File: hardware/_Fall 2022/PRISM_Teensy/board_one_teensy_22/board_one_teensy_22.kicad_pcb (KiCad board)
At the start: 2 copper layers, 61 x 88.9 mm, 20 parts, among them J1 EAST, J2 CORE_IO, J3 USB_micro, U1 Teensy4.1, U2 BNO055_Breakout, U3 3966

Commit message: minor fixes
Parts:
- moved ? 0.25 mm to (138.2, 134.6)
- moved H3 0.10 mm to (156.7, 53.2)
- moved H4 0.09 mm to (118.6, 135.8)
- moved H2 0.09 mm to (156.7, 135.8)
- moved H1 0.08 mm to (118.6, 53.3)
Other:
- outline, holes or cut-outs redrawn
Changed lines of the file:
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@@
     (descr "Resistor SMD 0603 (1608 Metric), square (rectangular) end terminal, IPC_7351 nominal, (Body size source: IPC-SM-782 page 72, https://www.pcb-3d.com/wordpress/wp-content/uploads/ipc-sm-782a_amendment_1_and_2.pdf), generated with kicad-footprint-generator")
     (tags "resistor")
-    (property "JLC" "C473494")
     (property "Sheetfile" "board_one_teensy_22.kicad_sch")
     (property "Sheetname" "")
+    (property "Vendor" "C23024")
     (attr smd)
     (fp_text reference "R5" (at 0 -1.43 90) (layer "F.SilkS") hide
@@
     (property "sensor output" "I2C,SPI")
     (attr through_hole)
-    (fp_text reference "U3" (at -12.7 -9.69 90) (layer "F.SilkS")
+    (fp_text reference "U3" (at -5.332 -0.048 90) (layer "F.SilkS")
       (effects (font (size 1 1) (thickness 0.15)) (justify left))
     )
@@
   )
   (footprint "MountingHole:MountingHole_3.2mm_M3_DIN965_Pad_TopBottom" (layer "F.Cu")
-    (at 118.618 53.34)
+    (at 118.614971 53.255682)
     (descr "Mounting Hole 3.2mm, M3, DIN965")
     (tags "mounting hole 3.2mm m3 din965")
@@
     (property "Sheetname" "")
     (attr through_hole)
-    (fp_text reference "J2" (at 3.275 -4.765 90) (layer "F.SilkS")
-      (effects (font (size 1 1) (thickness 0.15)))
-    )
-    (fp_text value "CORE_IO" (at 6 7.45 90) (layer "F.Fab")
+    (fp_text reference "J2" (at -3.724 2.758 90) (layer "F.SilkS")
+      (effects (font (size 1 1) (thickness 0.15)))
+    )
+    (fp_text value "CORE_IO" (at 6 7.838 90) (layer "F.SilkS")
       (effects (font (size 1 1) (thickness 0.15)))
     )
@@
     (descr "Capacitor SMD 0603 (1608 Metric), square (rectangular) end terminal, IPC_7351 nominal, (Body size source: IPC-SM-782 page 76, https://www.pcb-3d.com/wordpress/wp-content/uploads/ipc-sm-782a_amendment_1_and_2.pdf), generated with kicad-footprint-generator")
     (tags "capacitor")
-    (property "JLC" "C307380")
     (property "Sheetfile" "board_one_teensy_22.kicad_sch")
     (property "Sheetname" "")
+    (property "Vendor" "C14663")
     (attr smd)
     (fp_text reference "C2" (at 0 -1.43 90) (layer "F.SilkS") hide
@@
     (descr "Capacitor SMD 0603 (1608 Metric), square (rectangular) end terminal, IPC_7351 nominal, (Body size source: IPC-SM-782 page 76, https://www.pcb-3d.com/wordpress/wp-content/uploads/ipc-sm-782a_amendment_1_and_2.pdf), generated with kicad-footprint-generator")
     (tags "capacitor")
-    (property "JLC" "C307380")
     (property "Sheetfile" "board_one_teensy_22.kicad_sch")
     (property "Sheetname" "")
+    (property "Vendor" "C14663")
     (attr smd)
     (fp_text reference "C1" (at 0 -1.43 -90) (layer "F.SilkS") hide
@@
     (descr "SOT, 3 Pin (https://www.jedec.org/system/files/docs/to-236h.pdf variant AB), generated with kicad-footprint-generator ipc_gullwing_generator.py")
     (tags "SOT TO_SOT_SMD")
-    (property "JLC" "C369922")
     (property "Sheetfile" "board_one_teensy_22.kicad_sch")
     (property "Sheetname" "")
+    (property "Vendor" "C369922")
     (attr smd)
     (fp_text reference "D1" (at 0 -2.4 90) (layer "F.SilkS")
@@
   )
   (footprint "MountingHole:MountingHole_3.2mm_M3_DIN965_Pad_TopBottom" (layer "F.Cu")
-    (at 118.618 135.89)
+    (at 118.603304 135.797904)
     (descr "Mounting Hole 3.2mm, M3, DIN965")
     (tags "mounting hole 3.2mm m3 din965")
@@
     (property "Sheetname" "")
     (attr exclude_from_pos_files)
-    (fp_text reference "H4" (at 0 -3.8) (layer "User.1")
+    (fp_text reference "H4" (at 0 6.950096) (layer "User.1")
       (effects (font (size 1 1) (thickness 0.15)))
     )
@@
   )
   (footprint "MountingHole:MountingHole_3.2mm_M3_DIN965_Pad_TopBottom" (layer "F.Cu")
-    (at 156.718 53.34)
+    (at 156.706146 53.242782)
     (descr "Mounting Hole 3.2mm, M3, DIN965")
     (tags "mounting hole 3.2mm m3 din965")
@@
     (property "Sheetname" "")
     (attr through_hole)
-    (fp_text reference "U2" (at 0 -11.565 90) (layer "F.SilkS")
+    (fp_text reference "U2" (at 0 -0.386 90) (layer "F.SilkS")
       (effects (font (size 1 1) (thickness 0.15)))
     )
@@
     (descr "Resistor SMD 0603 (1608 Metric), square (rectangular) end terminal, IPC_7351 nominal, (Body size source: IPC-SM-782 page 72, https://www.pcb-3d.com/wordpress/wp-content/uploads/ipc-sm-782a_amendment_1_and_2.pdf), generated with kicad-footprint-generator")
     (tags "resistor")
-    (property "JLC" "C163495")
     (property "Sheetfile" "board_one_teensy_22.kicad_sch")
     (property "Sheetname" "")
+    (property "Vendor" "C25811")
     (attr smd)
     (fp_text reference "R4" (at 0 -1.43 -90) (layer "F.SilkS") hide
@@
   )
   (footprint "MountingHole:MountingHole_3.2mm_M3_DIN965_Pad_TopBottom" (layer "F.Cu")
-    (at 156.718 135.89)
+    (at 156.701211 135.804448)
     (descr "Mounting Hole 3.2mm, M3, DIN965")
     (tags "mounting hole 3.2mm m3 din965")
@@
     (property "Sheetname" "")
     (attr exclude_from_pos_files)
-    (fp_text reference "H2" (at 0 -3.8) (layer "User.1")
+    (fp_text reference "H2" (at 0.524789 6.181552) (layer "User.1")
       (effects (font (size 1 1) (thickness 0.15)))
     )
@@
   )
   (footprint "LOGO" (layer "F.Cu")
-    (at 138.43 134.62)
+    (at 138.176 134.62)
     (attr board_only exclude_from_pos_files exclude_from_bom)
     (fp_text reference "" (at 0 0) (layer "F.SilkS")
@@
     (property "Sheetname" "")
     (attr through_hole)
-    (fp_text reference "U1" (at 0 -10.16 90) (layer "F.SilkS")
+    (fp_text reference "U1" (at 6.866 -0.113 90) (layer "F.SilkS")
       (effects (font (size 1 1) (thickness 0.15)))
     )
@@
       (effects (font (size 1 1) (thickness 0.15)))
     )
-    (fp_text value "EAST" (at 3 7.45) (layer "F.Fab")
+    (fp_text value "EAST" (at 3 8.122) (layer "F.SilkS")
       (effects (font (size 1 1) (thickness 0.15)))
     )
@@
   )
   (gr_line (start 163.28 102.04) (end 163.28 127.44) (layer "Dwgs.User") (width 0.2))
+  (gr_circle (center 156.71 135.8) (end 158.54642 135.8) (layer "Dwgs.User") (width 0.2) (fill none))
   (gr_line (start 145.5 102.04) (end 163.28 102.04) (layer "Dwgs.User") (width 0.2))
+  (gr_circle (center 156.71 53.25) (end 158.54642 53.25) (layer "Dwgs.User") (width 0.2) (fill none))
   (gr_line (start 145.5 71.37) (end 165.82 71.37) (layer "Dwgs.User") (width 0.2))
+  (gr_circle (center 118.61 53.25) (end 120.44642 53.25) (layer "Dwgs.User") (width 0.2) (fill none))
   (gr_line (start 145.5 127.44) (end 145.5 102.04) (layer "Dwgs.User") (width 0.2))
   (gr_line (start 165.82 71.37) (end 165.82 98.04) (layer "Dwgs.User") (width 0.2))
@@
   (gr_line (start 119.72 86.075) (end 119.72 102.975) (layer "Dwgs.User") (width 0.2))
   (gr_line (start 145.5 98.04) (end 145.5 71.37) (layer "Dwgs.User") (width 0.2))
+  (gr_circle (center 118.61 135.8) (end 120.44642 135.8) (layer "Dwgs.User") (width 0.2) (fill none))
   (gr_line (start 111.12 102.975) (end 111.12 86.075) (layer "Dwgs.User") (width 0.2))
   (gr_line (start 141.5 119.73) (end 141.5 58.77) (layer "Dwgs.User") (width 0.2))
@@
   (gr_line (start 119.72 102.975) (end 111.12 102.975) (layer "Dwgs.User") (width 0.2))
   (gr_line (start 165.82 98.04) (end 145.5 98.04) (layer "Dwgs.User") (width 0.2))
-  (gr_circle (center 156.71 135.8) (end 158.54642 135.8) (layer "Edge.Cuts") (width 0.2) (fill none))
   (gr_line (start 142.61 123.23) (end 142.61 127.484) (layer "Edge.Cuts") (width 0.2))
   (gr_arc (start 130.11 127.484) (mid 129.23132 129.60532) (end 127.11 130.484) (layer "Edge.Cuts") (width 0.2))
   (gr_line (start 168.14 136.435) (end 168.14 52.615) (layer "Edge.Cuts") (width 0.2))
-  (gr_circle (center 156.71 53.25) (end 158.54642 53.25) (layer "Edge.Cuts") (width 0.2) (fill none))
   (gr_line (start 125.61 130.484) (end 127.11 130.484) (layer "Edge.Cuts") (width 0.2))
-  (gr_circle (center 118.61 53.25) (end 120.44642 53.25) (layer "Edge.Cuts") (width 0.2) (fill none))
   (gr_line (start 109.72 138.975) (end 165.6 138.975) (layer "Edge.Cuts") (width 0.2))
   (gr_line (start 139.61 120.23) (end 138.11 120.23) (layer "Edge.Cuts") (width 0.2))
@@
   (gr_arc (start 122.61 123.23) (mid 123.48868 121.10868) (end 125.61 120.23) (layer "Edge.Cuts") (width 0.2))
   (gr_line (start 130.11 123.23) (end 130.11 127.484) (layer "Edge.Cuts") (width 0.2))
-  (gr_circle (center 118.61 135.8) (end 120.44642 135.8) (layer "Edge.Cuts") (width 0.2) (fill none))
   (gr_line (start 122.61 127.484) (end 122.61 123.23) (layer "Edge.Cuts") (width 0.2))
   (gr_arc (start 109.72 138.975) (mid 107.923949 138.231051) (end 107.18 136.435) (layer "Edge.Cuts") (width 0.2))

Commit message: Board one complete
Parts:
- added D2: SS54, JLC_footprints:DO-214AC, F.Cu at (162.3, 61.0)
- D1: value BAT54C -> SS54; footprint Package_TO_SOT_SMD:SOT-23 -> JLC_footprints:DO-214AC
- moved D1 5.01 mm to (162.3, 65.3), turned to 180 degrees
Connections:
- U1 pad 12: /CS -> unconnected-(U1-Pad12)
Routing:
- net /VIN: track 27.0 -> 36.9 mm
- net /V_BATT: track 79.5 -> 76.3 mm
- net /V_USB: track 52.3 -> 54.2 mm

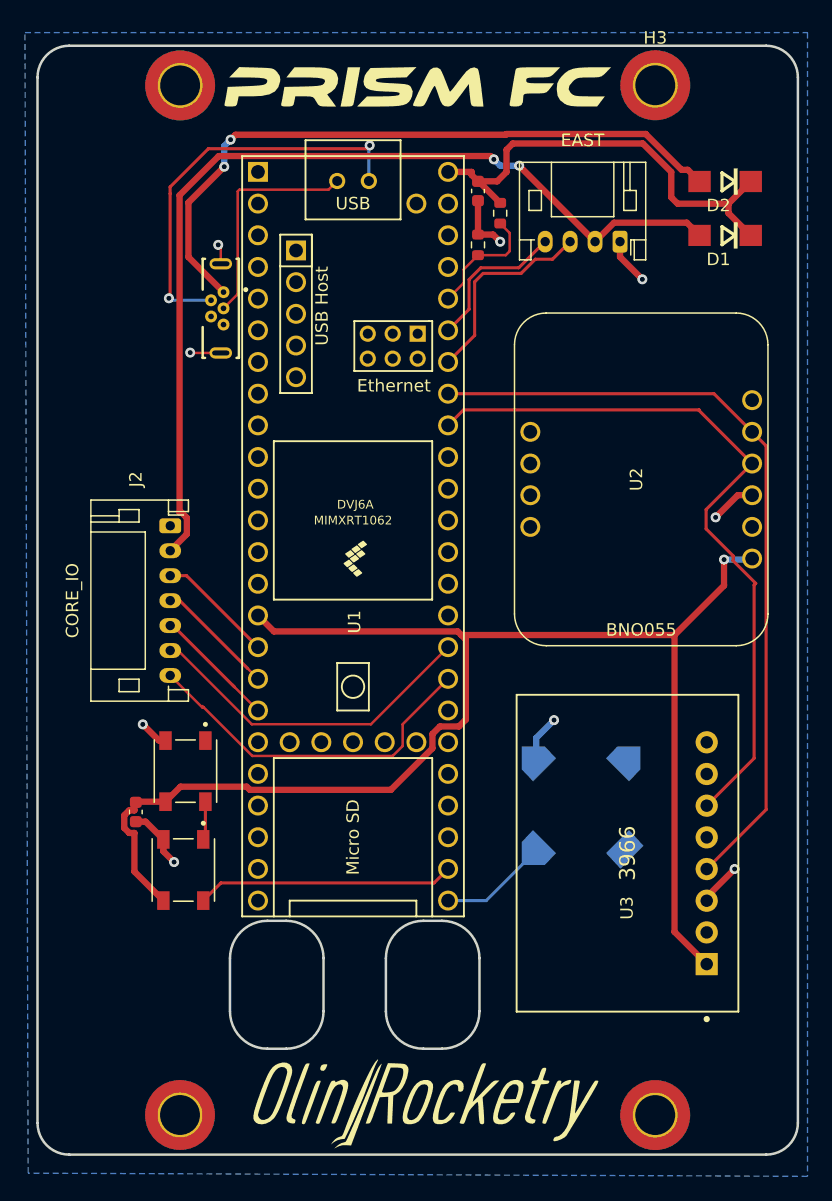
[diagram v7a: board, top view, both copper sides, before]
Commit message: fix DRC errors on PRISM FC
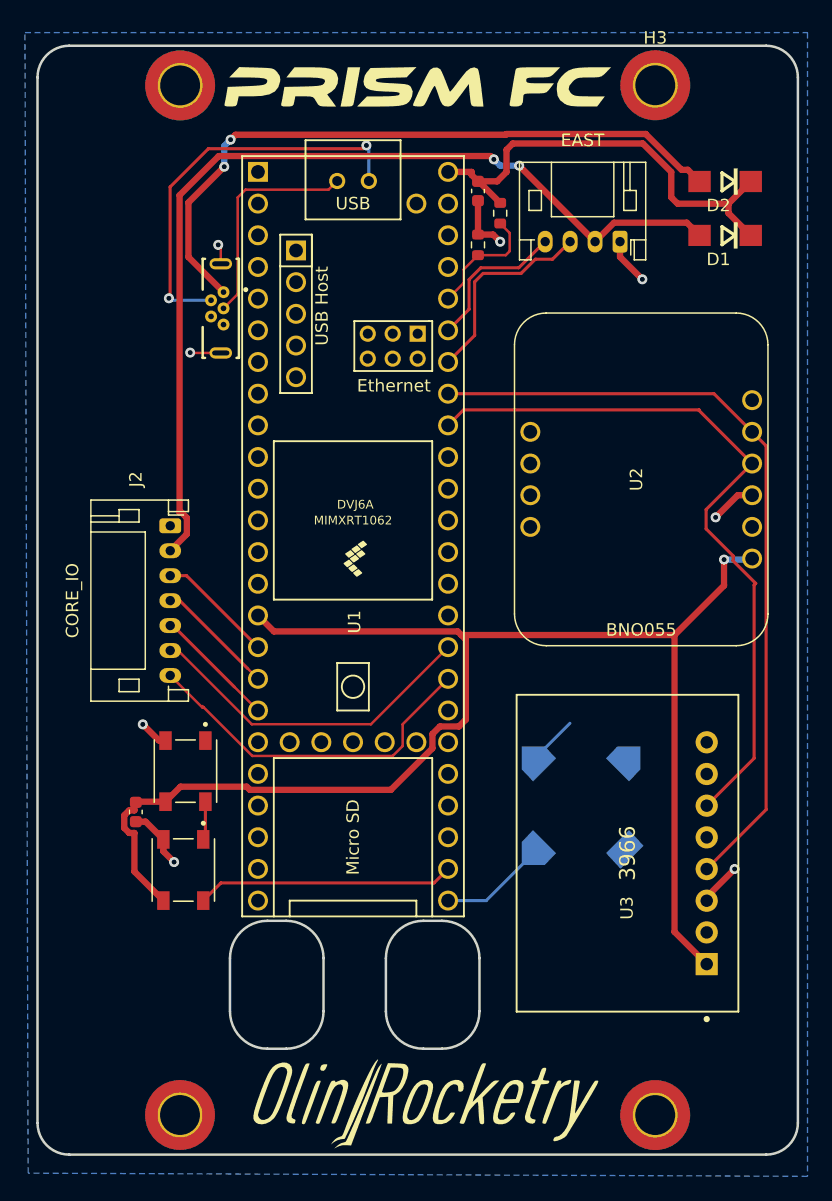
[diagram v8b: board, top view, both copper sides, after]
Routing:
- net /PYRO 1: track 11.0 -> 9.41 mm
- net /PYRO 2: track 10.6 -> 9.63 mm
- net Net-(J3-Pad3): track 18.7 -> 17.9 mm
- net GND: track 30.9 -> 31.2 mm, vias 9 -> 8
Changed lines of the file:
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@@
   (segment (start 153.88 67.01) (end 155.67 68.8) (width 0.508) (layer "F.Cu") (net 2))
   (segment (start 143.701 65.215) (end 142.494 65.215) (width 0.508) (layer "F.Cu") (net 2))
-  (via (at 148.59 104.14) (size 0.8) (drill 0.4) (layers "F.Cu" "B.Cu") (net 2))
   (via (at 163.068 116.078) (size 0.8) (drill 0.4) (layers "F.Cu" "B.Cu") (net 2))
   (via (at 118.13 115.52) (size 0.8) (drill 0.4) (layers "F.Cu" "B.Cu") (net 2))
@@
   (via (at 121.666 66.04) (size 0.8) (drill 0.4) (layers "F.Cu" "B.Cu") (net 2))
   (segment (start 119.4207 74.676) (end 119.38 74.7167) (width 0.2032) (layer "B.Cu") (net 2))
-  (segment (start 147.15825 107.402) (end 147.15825 105.57175) (width 0.508) (layer "B.Cu") (net 2))
-  (segment (start 147.15825 105.57175) (end 148.59 104.14) (width 0.508) (layer "B.Cu") (net 2))
+  (segment (start 147.15825 107.09575) (end 149.86 104.394) (width 0.25) (layer "B.Cu") (net 2))
+  (segment (start 147.15825 107.402) (end 147.15825 107.09575) (width 0.25) (layer "B.Cu") (net 2))
   (segment (start 149.88 65.78) (end 148.47211 67.18789) (width 0.25) (layer "F.Cu") (net 3))
   (segment (start 147.08789 67.18789) (end 145.94978 68.326) (width 0.25) (layer "F.Cu") (net 3))
@@
   (segment (start 119.125 92.56) (end 124.855 98.29) (width 0.25) (layer "F.Cu") (net 4))
   (segment (start 117.82 92.56) (end 119.125 92.56) (width 0.25) (layer "F.Cu") (net 4))
-  (segment (start 123.7534 97.1884) (end 124.855 98.29) (width 0.2032) (layer "F.Cu") (net 4))
-  (segment (start 123.3502 99.3252) (end 124.0325 100.0075) (width 0.2032) (layer "F.Cu") (net 5))
   (segment (start 117.82 94.56) (end 118.585 94.56) (width 0.25) (layer "F.Cu") (net 5))
   (segment (start 118.585 94.56) (end 124.0325 100.0075) (width 0.25) (layer "F.Cu") (net 5))
@@
   (segment (start 124.398702 107.0116) (end 135.66 107.0116) (width 0.2032) (layer "F.Cu") (net 7))
   (segment (start 135.66 107.0116) (end 136.4534 106.2182) (width 0.2032) (layer "F.Cu") (net 7))
-  (segment (start 122.7836 101.2986) (end 122.9675 101.4825) (width 0.2032) (layer "F.Cu") (net 8))
   (segment (start 118.045 96.56) (end 122.9675 101.4825) (width 0.25) (layer "F.Cu") (net 8))
   (segment (start 117.82 96.56) (end 118.045 96.56) (width 0.25) (layer "F.Cu") (net 8))
@@
   (segment (start 145.288 57.912) (end 155.704236 57.912) (width 0.508) (layer "F.Cu") (net 69))
   (segment (start 140.095 60.19) (end 141.979 60.19) (width 0.508) (layer "F.Cu") (net 69))
-  (segment (start 164.356 60.96) (end 164.592 60.96) (width 0.25) (layer "F.Cu") (net 69))
   (segment (start 142.494 60.947) (end 142.544 60.947) (width 0.508) (layer "F.Cu") (net 69))
   (segment (start 157.988 62.23) (end 158.496 62.738) (width 0.508) (layer "F.Cu") (net 69))
@@
   (segment (start 122.15 59.7735) (end 122.15 58.1155) (width 0.508) (layer "B.Cu") (net 70))
   (segment (start 122.15 58.1155) (end 122.66 57.6055) (width 0.508) (layer "B.Cu") (net 70))
-  (segment (start 133.5465 58.33) (end 120.88 58.33) (width 0.25) (layer "F.Cu") (net 72))
-  (segment (start 117.81 61.93) (end 117.81 70.2237) (width 0.25) (layer "F.Cu") (net 72))
   (segment (start 120.88 58.33) (end 117.81 61.4) (width 0.25) (layer "F.Cu") (net 72))
-  (segment (start 117.81 61.4) (end 117.81 61.93) (width 0.25) (layer "F.Cu") (net 72))
-  (segment (start 133.81 58.0665) (end 133.5465 58.33) (width 0.25) (layer "F.Cu") (net 72))
-  (segment (start 133.81 58.341) (end 133.81 58.0665) (width 0.25) (layer "F.Cu") (net 72))
   (segment (start 117.81 70.2237) (end 117.7137 70.32) (width 0.25) (layer "F.Cu") (net 72))
-  (via (at 133.81 58.0665) (size 0.8) (drill 0.4) (layers "F.Cu" "B.Cu") (net 72))
+  (segment (start 133.283 58.33) (end 120.88 58.33) (width 0.25) (layer "F.Cu") (net 72))
+  (segment (start 117.81 61.4) (end 117.81 70.2237) (width 0.25) (layer "F.Cu") (net 72))
+  (segment (start 133.5465 58.0665) (end 133.283 58.33) (width 0.25) (layer "F.Cu") (net 72))
+  (via (at 133.5465 58.0665) (size 0.8) (drill 0.4) (layers "F.Cu" "B.Cu") (net 72))
   (via (at 117.7137 70.32) (size 0.8) (drill 0.4) (layers "F.Cu" "B.Cu") (net 72))
-  (segment (start 133.81 58.0665) (end 133.745 58.1315) (width 0.25) (layer "B.Cu") (net 72))
+  (segment (start 133.745 60.92) (end 133.745 58.265) (width 0.25) (layer "B.Cu") (net 72))
   (segment (start 117.7137 70.32) (end 117.8737 70.48) (width 0.25) (layer "B.Cu") (net 72))
-  (segment (start 133.745 58.1315) (end 133.745 60.92) (width 0.25) (layer "B.Cu") (net 72))
+  (segment (start 133.745 58.265) (end 133.5465 58.0665) (width 0.25) (layer "B.Cu") (net 72))
   (segment (start 117.8737 70.48) (end 121.0925 70.48) (width 0.25) (layer "B.Cu") (net 72))
-  (segment (start 131.58 61.295) (end 131.205 60.92) (width 0.2032) (layer "F.Cu") (net 77))
-  (segment (start 123.23 61.74832) (end 123.23 69.9925) (width 0.2032) (layer "F.Cu") (net 77))
-  (segment (start 123.36416 61.61416) (end 123.23 61.74832) (width 0.2032) (layer "F.Cu") (net 77))
-  (segment (start 130.51084 61.61416) (end 131.205 60.92) (width 0.2032) (layer "F.Cu") (net 77))
-  (segment (start 123.36416 61.61416) (end 130.51084 61.61416) (width 0.2032) (layer "F.Cu") (net 77))
   (segment (start 123.23 69.9925) (end 122.0925 71.13) (width 0.2032) (layer "F.Cu") (net 77))
+  (segment (start 131.205 60.92) (end 130.51084 61.61416) (width 0.2032) (layer "F.Cu") (net 77))
+  (segment (start 123.85664 61.61416) (end 123.23 62.2408) (width 0.2032) (layer "F.Cu") (net 77))
+  (segment (start 123.23 62.2408) (end 123.23 69.9925) (width 0.2032) (layer "F.Cu") (net 77))
+  (segment (start 130.51084 61.61416) (end 123.85664 61.61416) (width 0.2032) (layer "F.Cu") (net 77))
   (zone (net 2) (net_name "GND") (layer "B.Cu") (hatch edge 0.508)
     (connect_pads (clearance 0.508))
